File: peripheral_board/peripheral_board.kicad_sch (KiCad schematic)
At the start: 0 parts

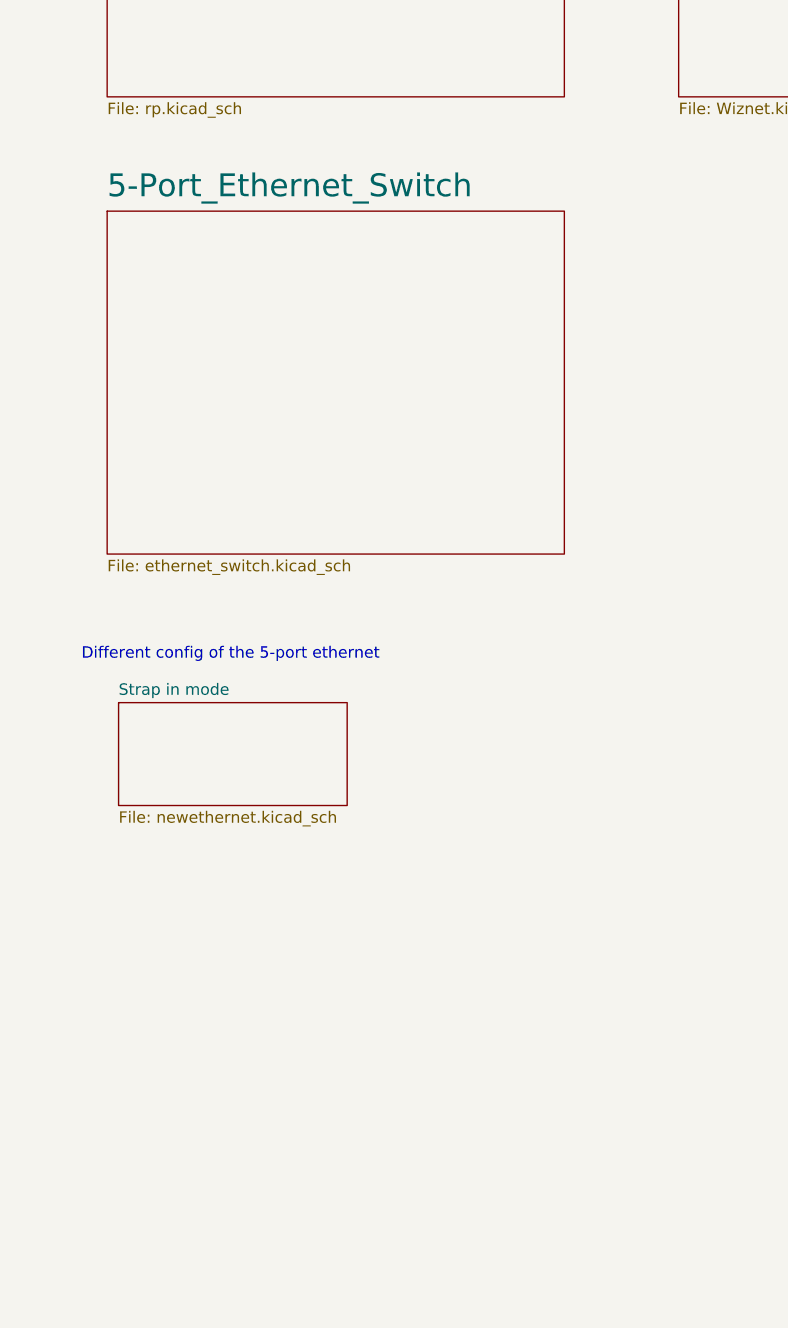
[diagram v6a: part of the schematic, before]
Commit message: Updated the PCB and the Schematic
Added in the strap in mode. Almost done with the RP schematic and the will then have to route signals.
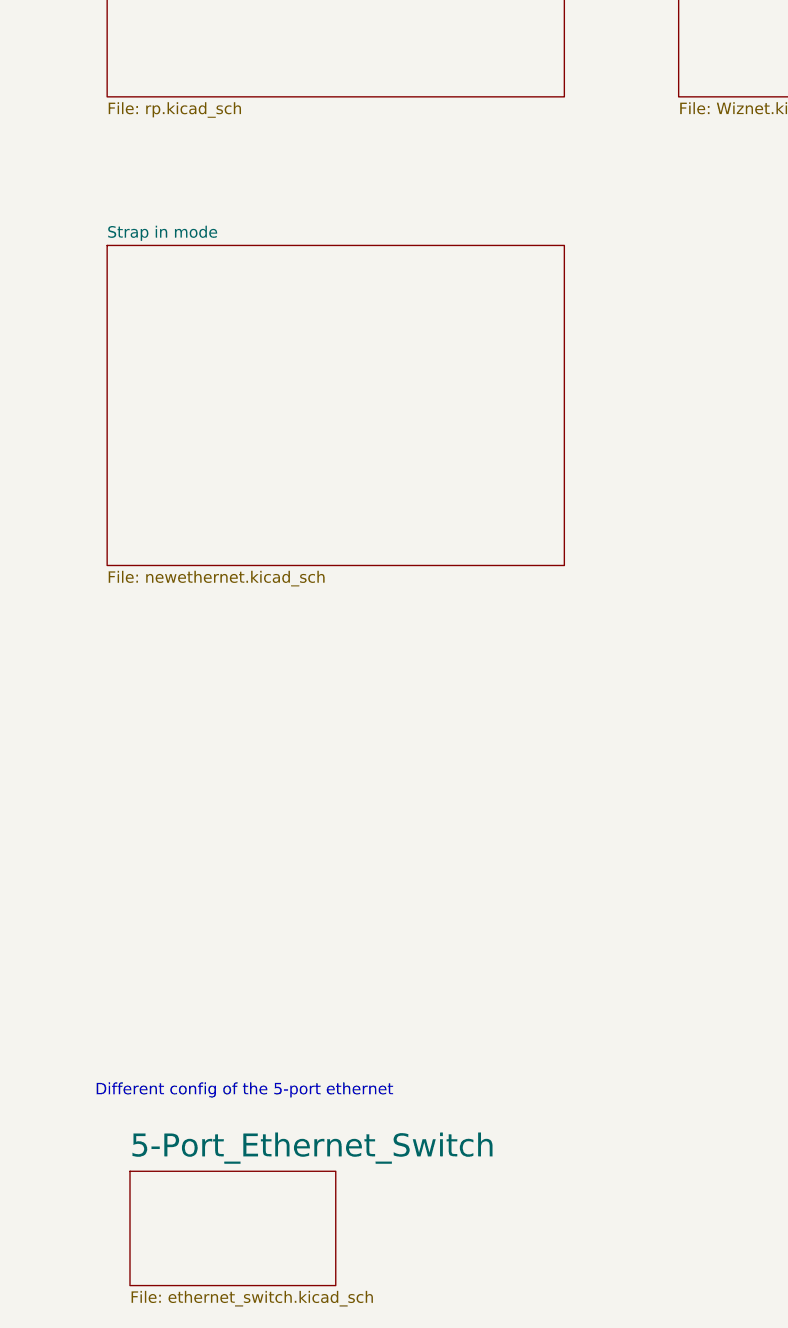
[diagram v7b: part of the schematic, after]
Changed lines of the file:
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@@
 	(text "Different config of the 5-port ethernet\n"
 		(exclude_from_sim no)
-		(at 39.116 125.476 0)
+		(at 40.64 173.99 0)
 		(effects
 			(font
@@
 	)
 	(sheet
-		(at 25.4 76.2)
-		(size 50.8 38.1)
-		(exclude_from_sim no)
-		(in_bom yes)
-		(on_board yes)
-		(dnp no)
+		(at 27.94 182.88)
+		(size 22.86 12.7)
+		(exclude_from_sim yes)
+		(in_bom no)
+		(on_board no)
+		(dnp yes)
 		(fields_autoplaced yes)
 		(stroke
@@
 		)
 		(property "Sheetname" "5-Port_Ethernet_Switch"
-			(at 25.4 74.8534 0)
+			(at 27.94 181.5334 0)
 			(effects
 				(font
@@
 		)
 		(property "Sheetfile" "ethernet_switch.kicad_sch"
-			(at 25.4 114.8846 0)
+			(at 27.94 196.1646 0)
 			(effects
 				(font
@@
 	)
 	(sheet
-		(at 26.67 130.81)
-		(size 25.4 11.43)
-		(exclude_from_sim yes)
-		(in_bom no)
-		(on_board no)
-		(dnp yes)
+		(at 25.4 80.01)
+		(size 50.8 35.56)
+		(exclude_from_sim no)
+		(in_bom yes)
+		(on_board yes)
+		(dnp no)
 		(fields_autoplaced yes)
 		(stroke
@@
 		)
 		(property "Sheetname" "Strap in mode"
-			(at 26.67 130.0984 0)
+			(at 25.4 79.2984 0)
 			(effects
 				(font
@@
 		)
 		(property "Sheetfile" "newethernet.kicad_sch"
-			(at 26.67 142.8246 0)
+			(at 25.4 116.1546 0)
 			(effects
 				(font

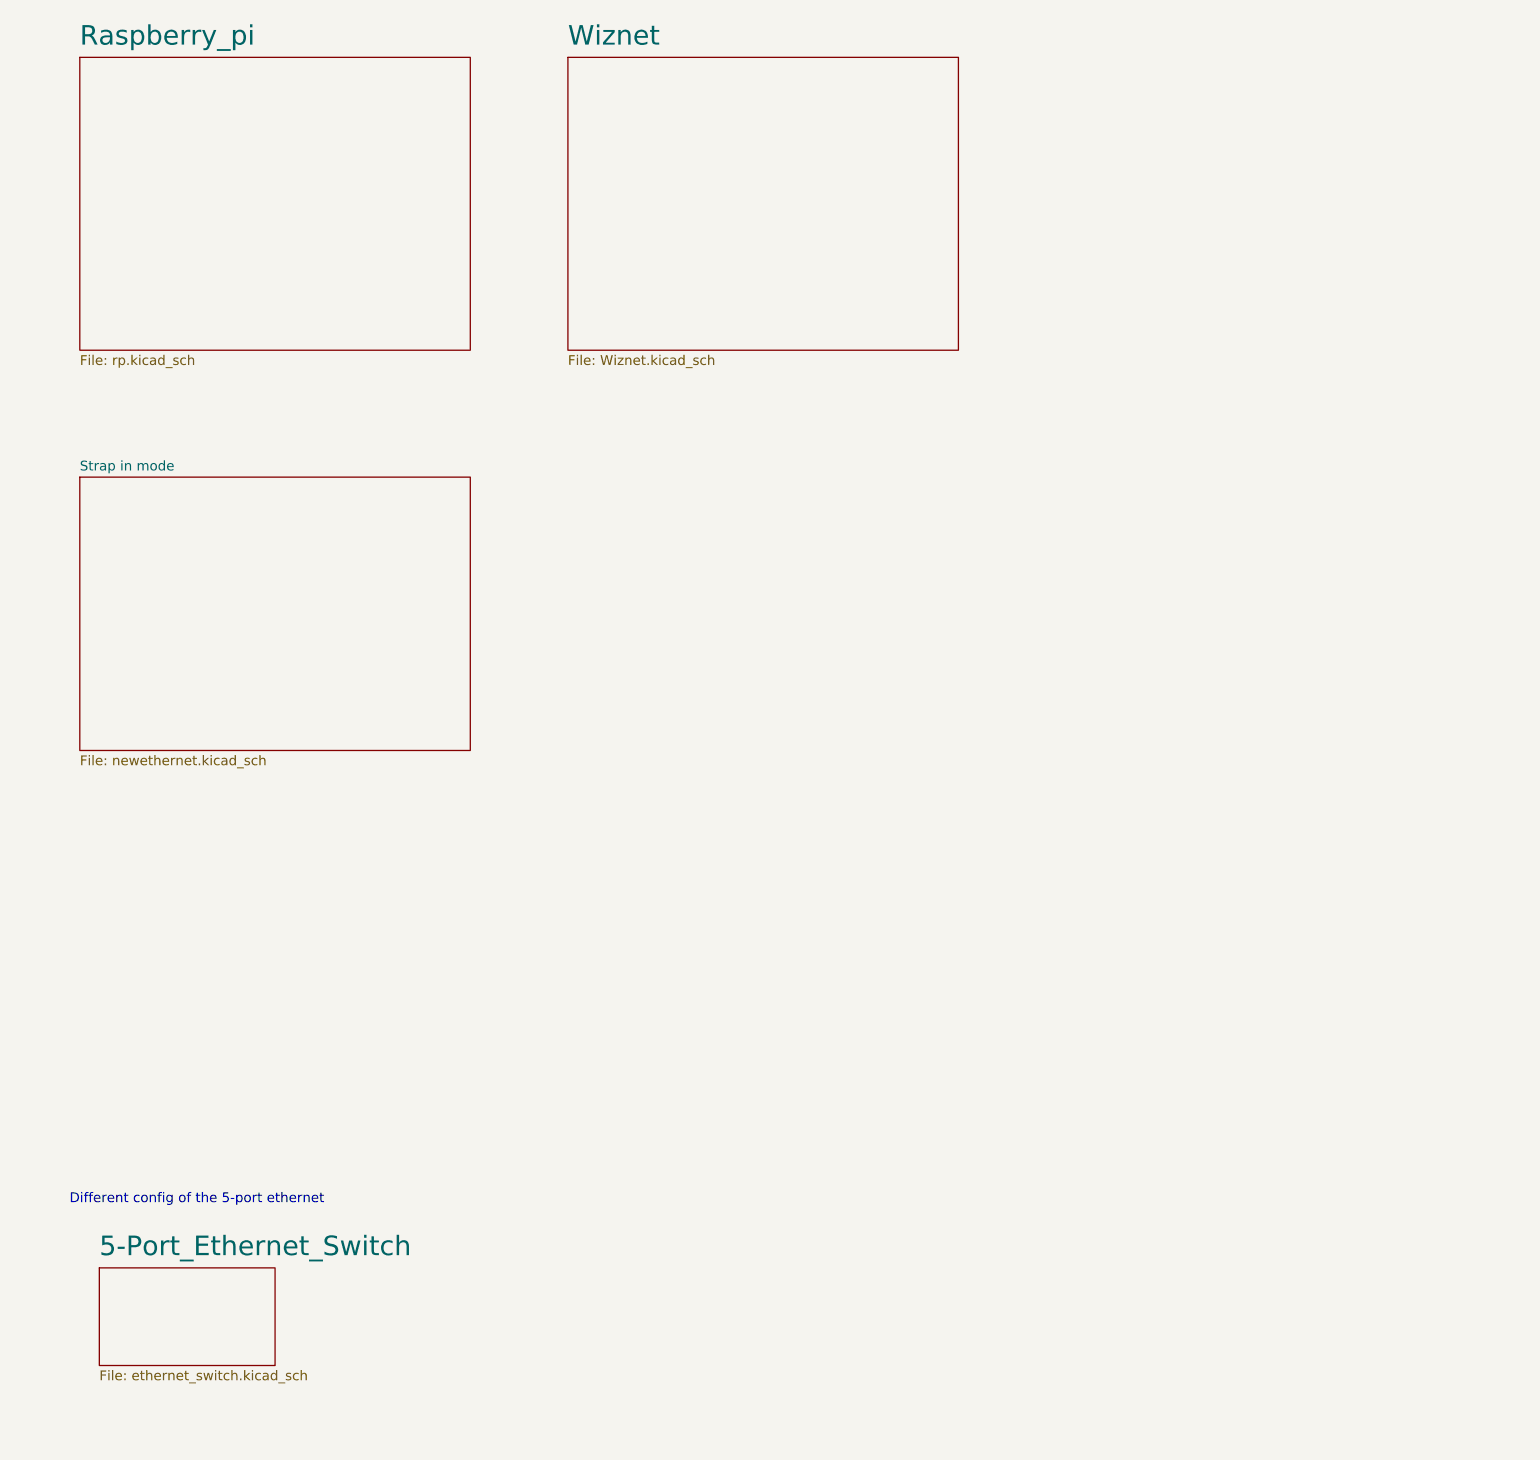
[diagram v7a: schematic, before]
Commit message: Added picture to create a block diagram
Placed pictures and wires with some text to give a block diagram.

Looked through the data sheets and found some info on the power for the ethernet switch. The power needs to go through a ferrite bead. Since we are getting power through a USB port I will use voltage regulators to get the 3.3V and the 1.2V needed for the board.

Tried to get the same version that we are using for the raspberry pi pico but the easyeda2kicad was not working. There is already one that was from the dev board that I have placed but I would like to keep the parts in the same family if possible.
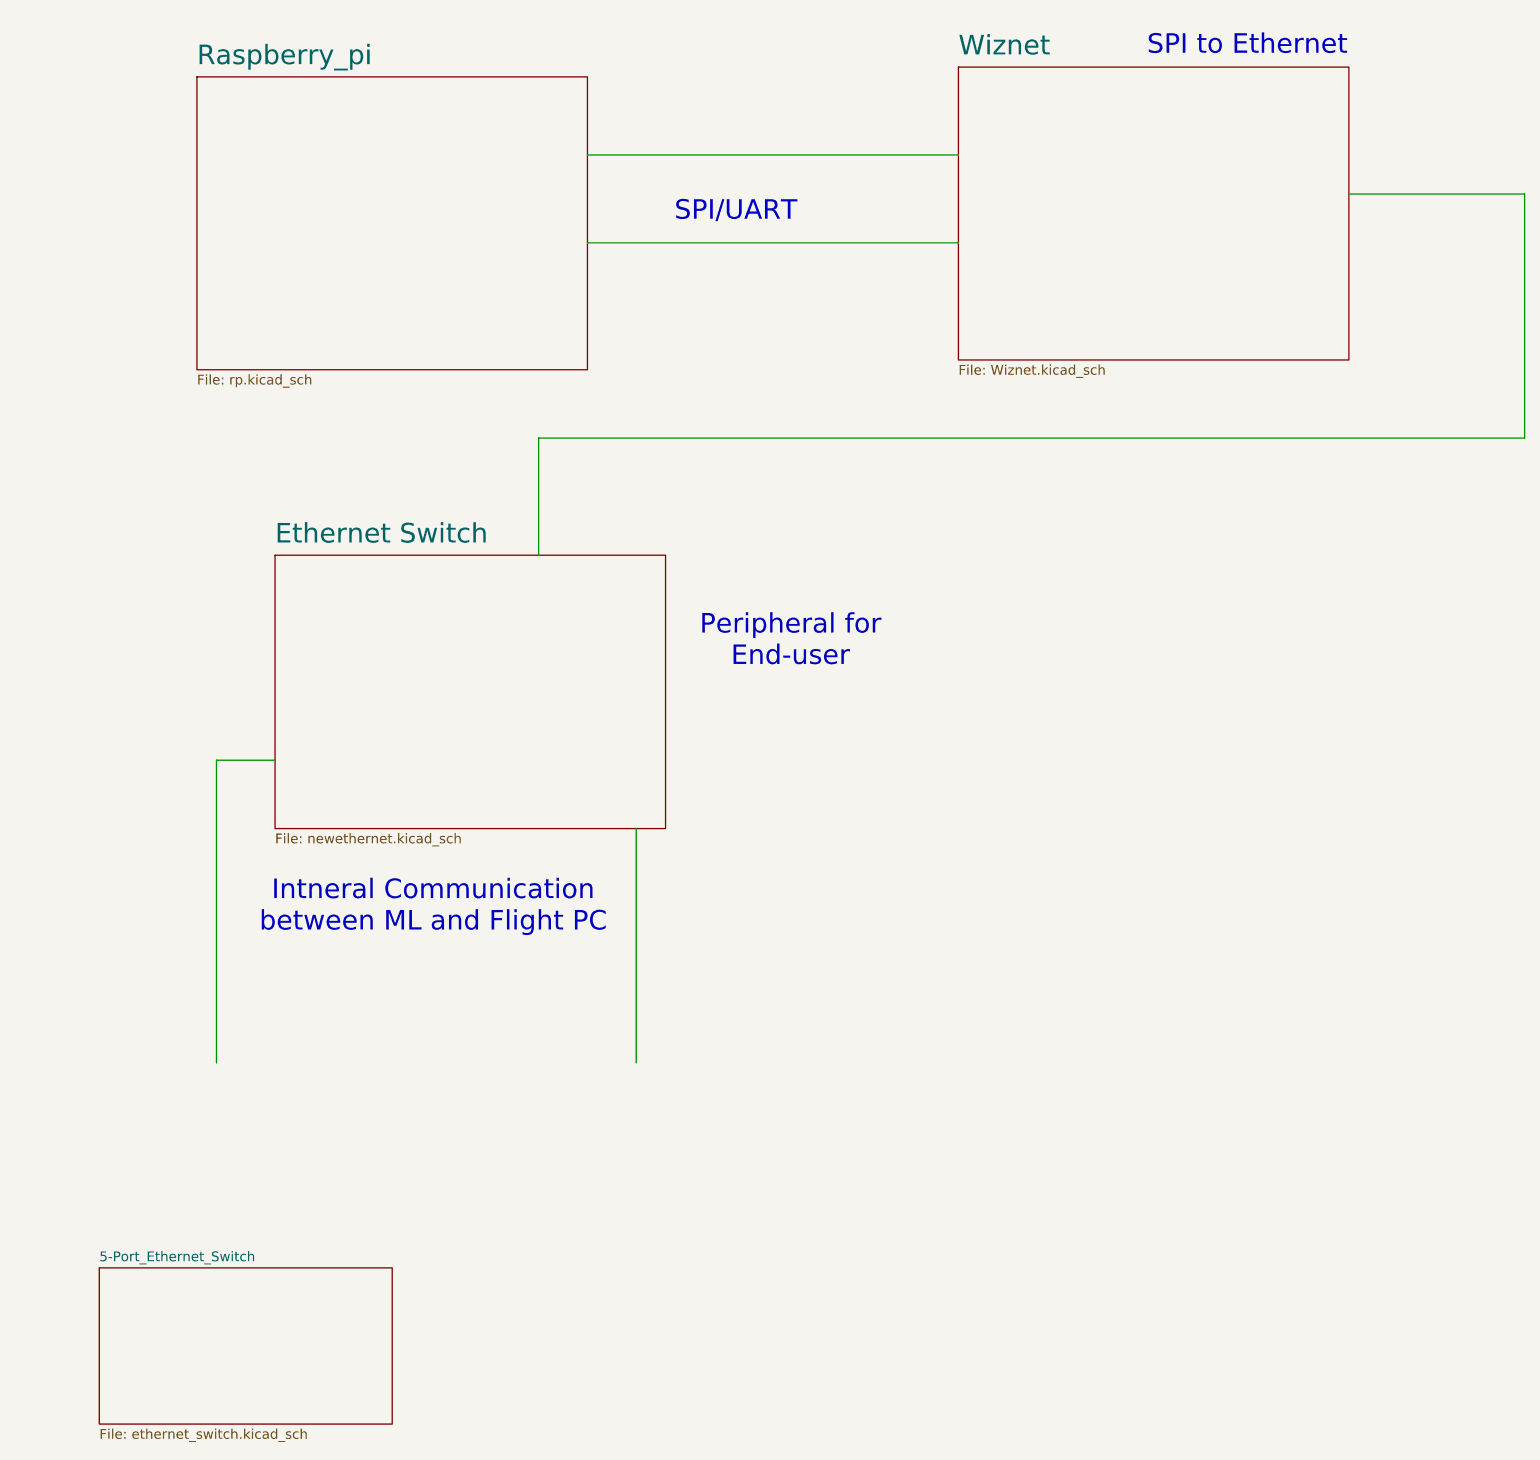
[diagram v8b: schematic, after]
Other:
- sheet Strap in mode renamed Ethernet Switch
- note added: "Intneral Communication between ML and Flight PC"
- note added: "Peripheral for End-user"
- note added: "SPI to Ethernet"
- note added: "SPI/UART"
- note removed: "Different config of the 5-port ethernet"
